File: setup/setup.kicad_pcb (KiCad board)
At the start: 2 copper layers, 54 x 94 mm, 19 parts, among them J1 Conn_01x08_Socket, J11 Motor Power, J2 Conn_01x08_Socket, J3 Step M1, J4 PS2 Controller, J5 Conn_01x22_Socket, J6 Conn_01x22_Socket, J7 6V IN, M1 Motor_Servo, M2 Motor_Servo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

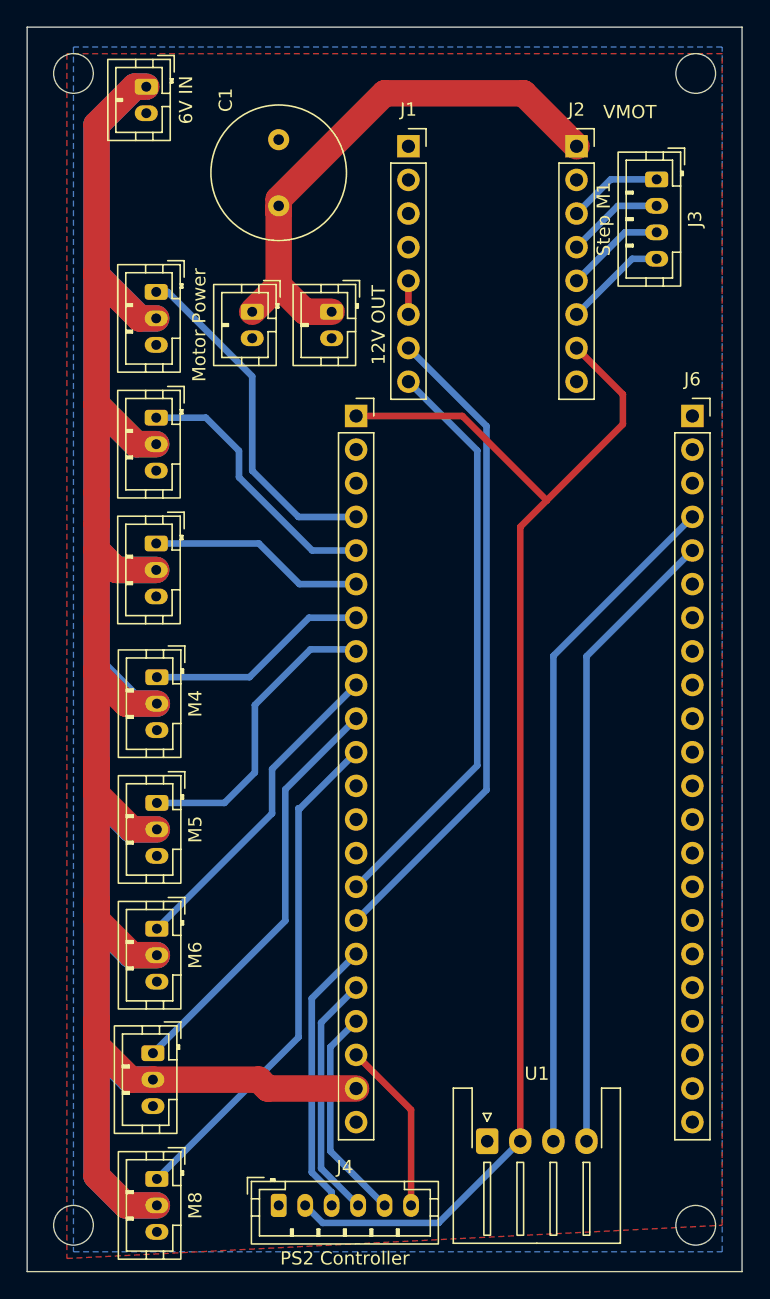
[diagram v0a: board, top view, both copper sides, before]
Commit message: feat: make board jlcpcb compatiable
Signed-off-by: kyle <kyle@nixos-desktop>
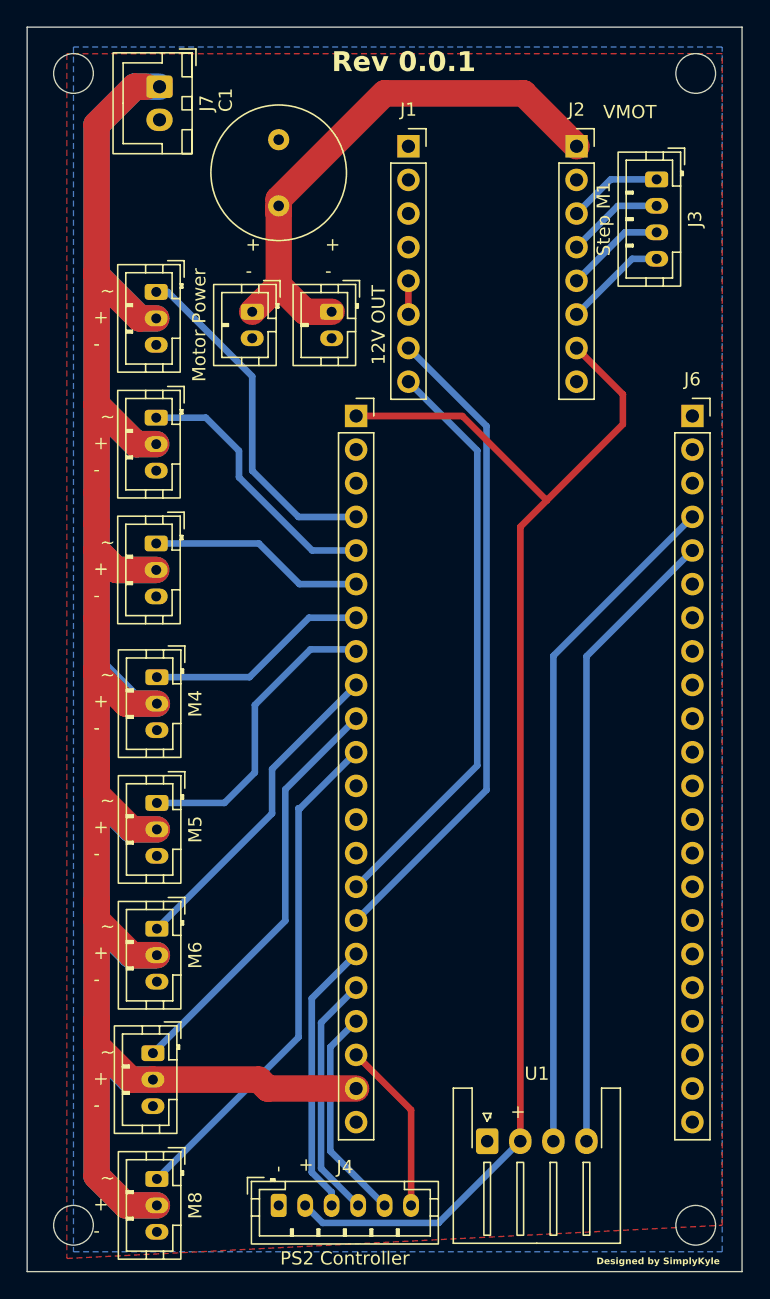
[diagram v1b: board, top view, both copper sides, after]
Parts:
- J7: footprint Connector_JST:JST_PH_B2B-PH-K_1x02_P2.00mm_Vertical -> Connector_JST:JST_XH_B2B-XH-A_1x02_P2.50mm_Vertical
- moved J7 1.00 mm to (125.0, 28.5)
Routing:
- net Net-(J5-5VIn): track 280.2 -> 281.2 mm
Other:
- copper layers 2 -> 4
- board text added: "+"
- board text added: "-"
- board text added: "Designed by SimplyKyle"
- board text added: "Rev 0.0.1"
- board text added: "~"

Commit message: feat: add jlcpcb & fix vh connection
Signed-off-by: kyle <kyle@nixos-portable>
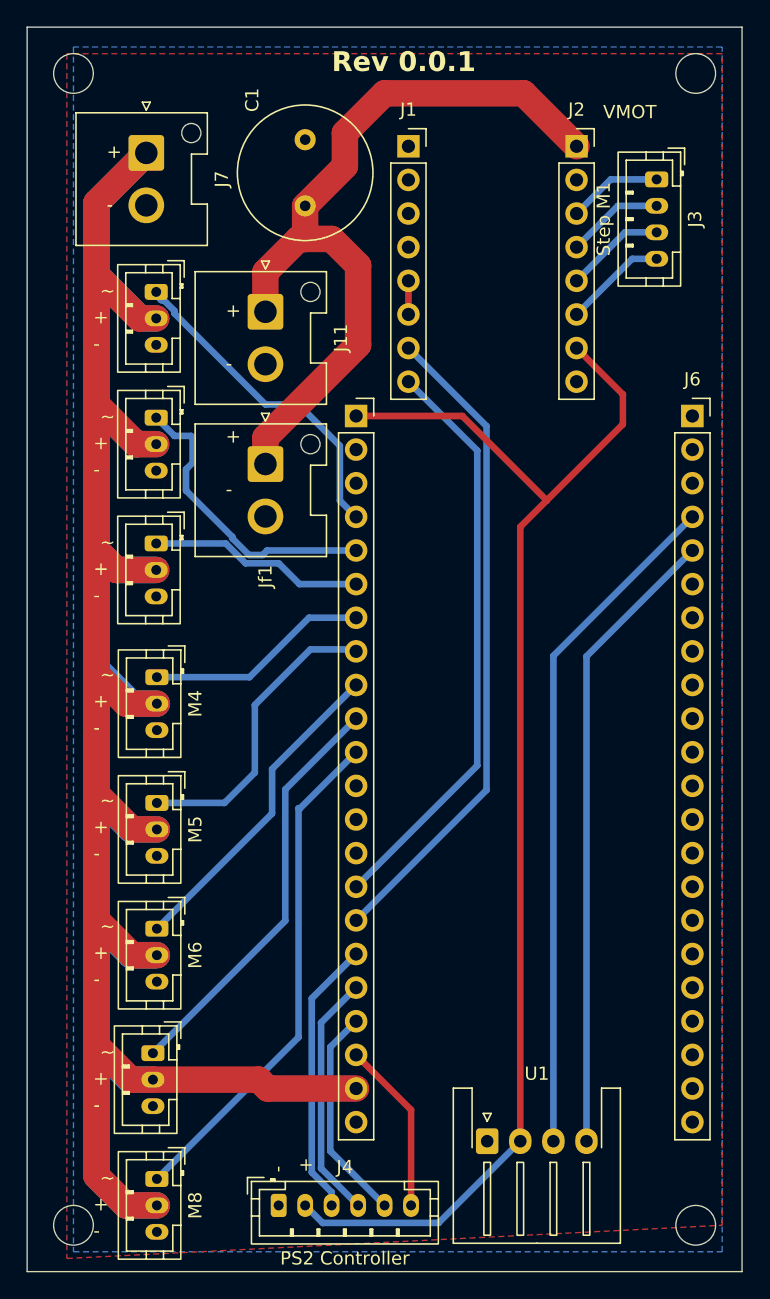
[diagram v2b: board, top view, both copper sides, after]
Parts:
- J11, Jf1: footprint Connector_JST:JST_PH_B2B-PH-K_1x02_P2.00mm_Vertical -> Connector_JST:JST_VH_B2P-VH-FB-B_1x02_P3.96mm_Vertical
- J7: footprint Connector_JST:JST_XH_B2B-XH-A_1x02_P2.50mm_Vertical -> Connector_JST:JST_VH_B2P-VH-FB-B_1x02_P3.96mm_Vertical
- moved Jf1 12.5 mm to (133.0, 57.0)
- moved J7 5.10 mm to (124.0, 33.5)
- moved C1 2.00 mm to (136.0, 37.5)
- moved J11 1.00 mm to (133.0, 45.5)
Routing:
- net Net-(J11-12V): track 42.1 -> 59.4 mm
- net Net-(J5-5VIn): track 281.2 -> 269.2 mm
- net Net-(M2-PWM): track 20.4 -> 22.7 mm
- net Net-(M1-PWM): track 26.3 -> 24.8 mm
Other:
- board text removed: "Designed by SimplyKyle"
